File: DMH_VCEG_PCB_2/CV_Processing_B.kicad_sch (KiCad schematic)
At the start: 58 parts, among them J26 Conn_01x10_PinHeader, Q27 BC558, Q28 BC558, Q29 BC548, Q30 BC548, Q31 BC548, Q32 BC548, U18 TL074, U19 TL074, U20 TL074

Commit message: Synced PCB 2 project with PCB 1
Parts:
- J26: footprint Connector_PinHeader_2.54mm:PinHeader_1x10_P2.54mm_Vertical -> Connector_PinSocket_2.54mm:PinSocket_1x10_P2.54mm_Vertical

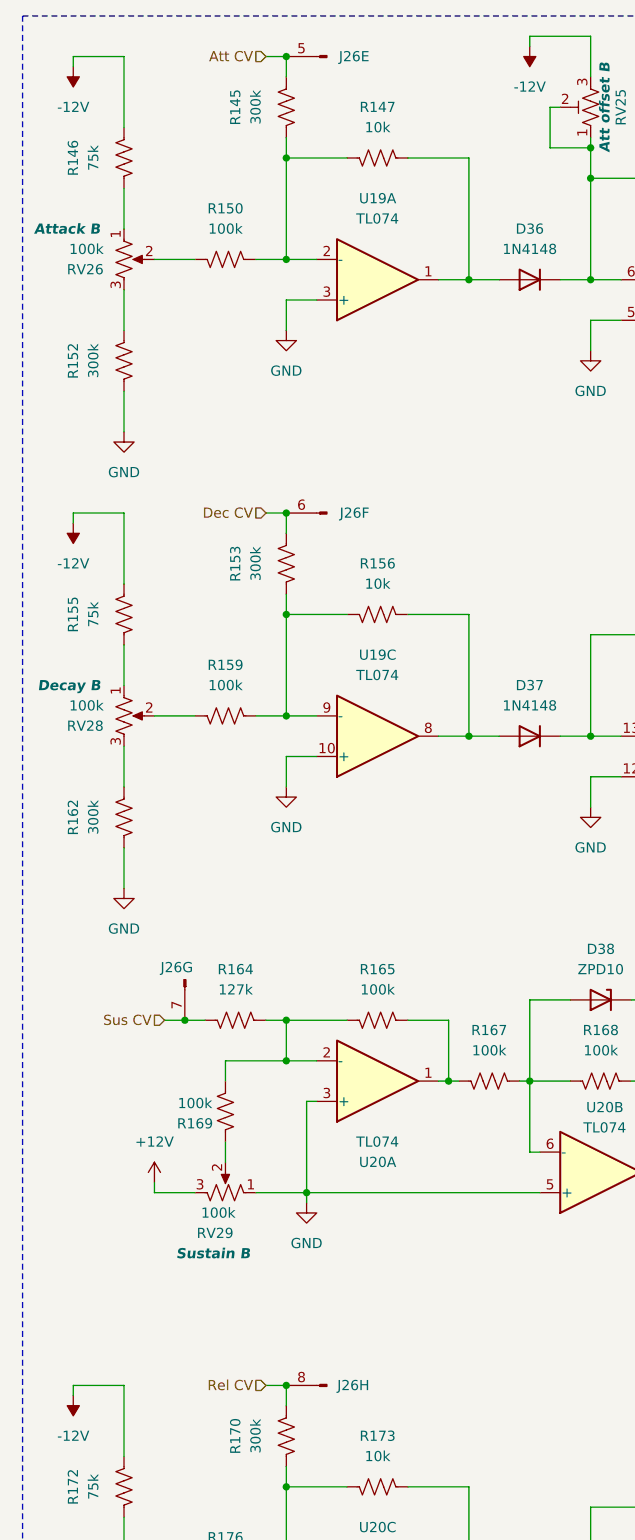
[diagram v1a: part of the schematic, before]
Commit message: PCB 2 placement in progress
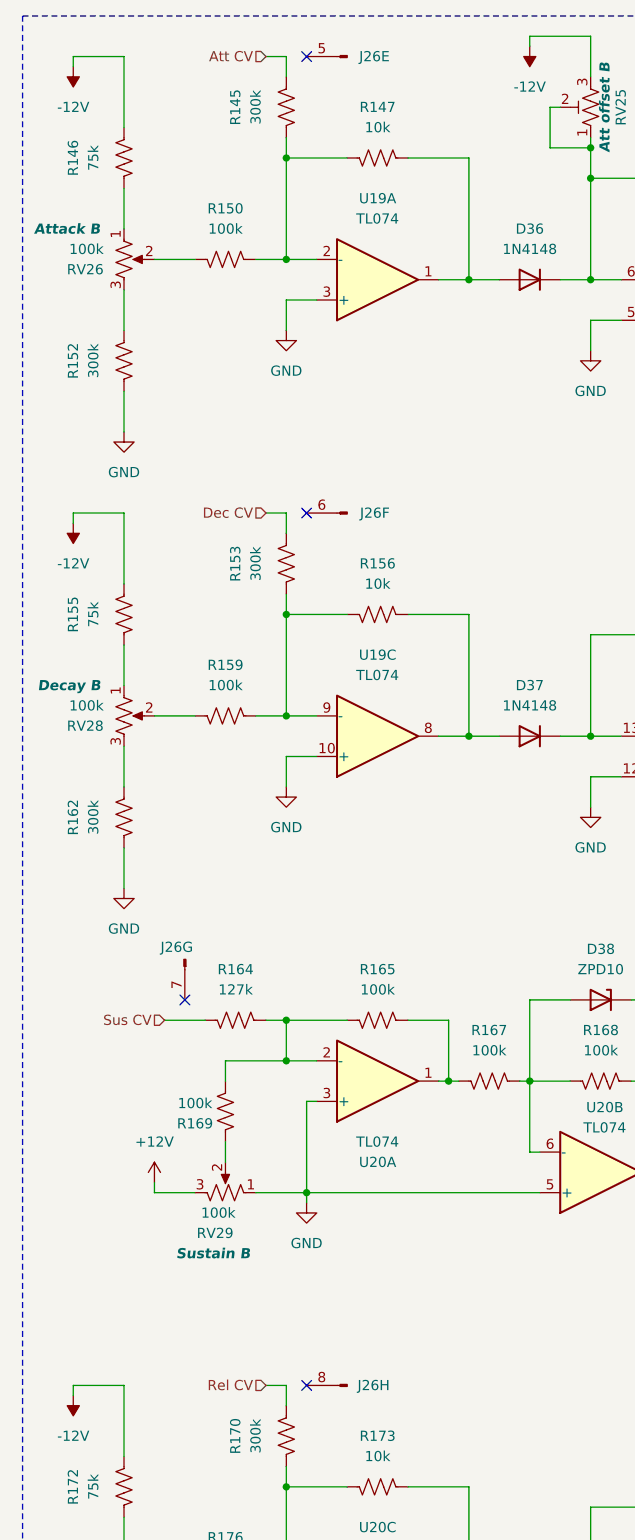
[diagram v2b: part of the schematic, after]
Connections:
- net Att CV: no longer J26.5 (Pin_5)
- net Dec CV: no longer J26.6 (Pin_6)
- net Rel CV: no longer J26.8 (Pin_8)
- net Sus CV: no longer J26.7 (Pin_7)
- no-connect marks 0 -> 4

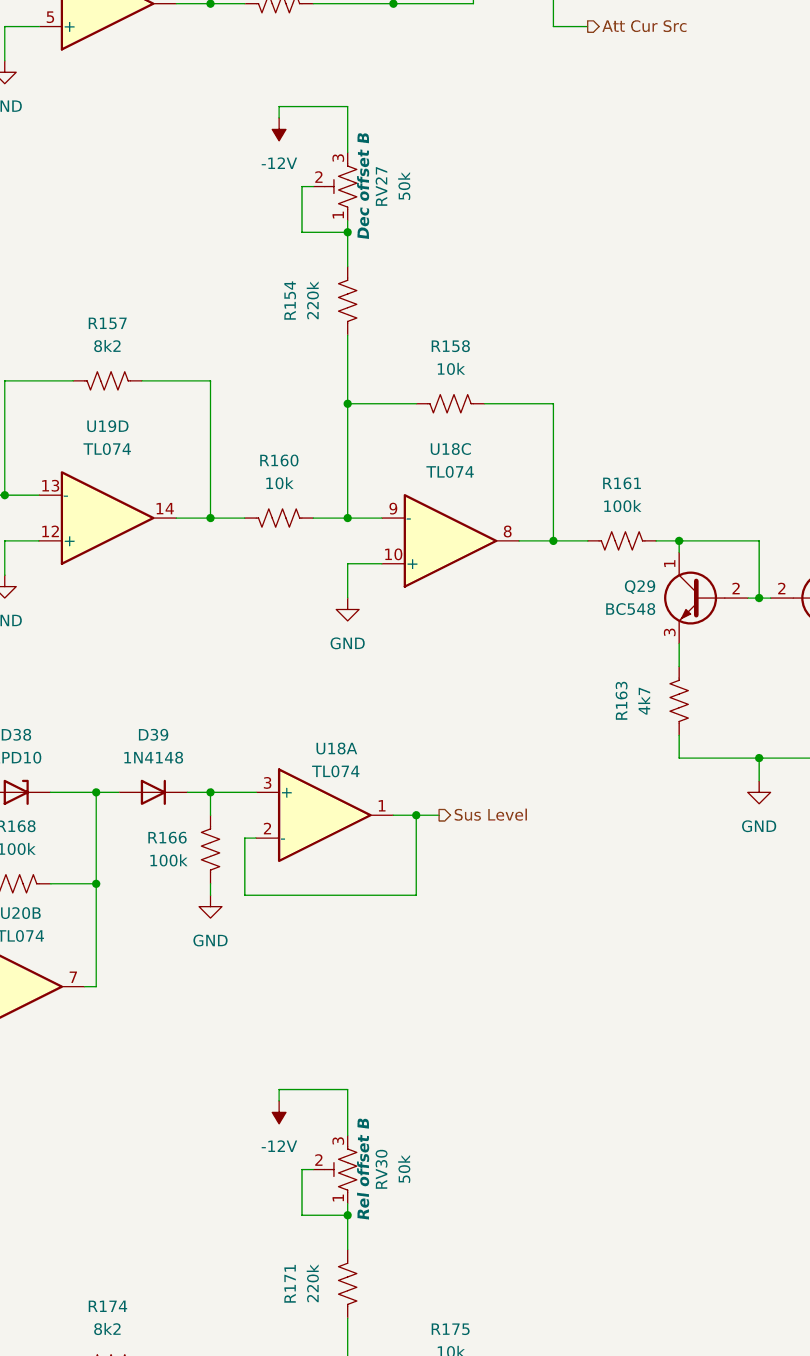
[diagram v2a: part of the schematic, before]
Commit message: Updated Dec and Rel trimpots to 100k
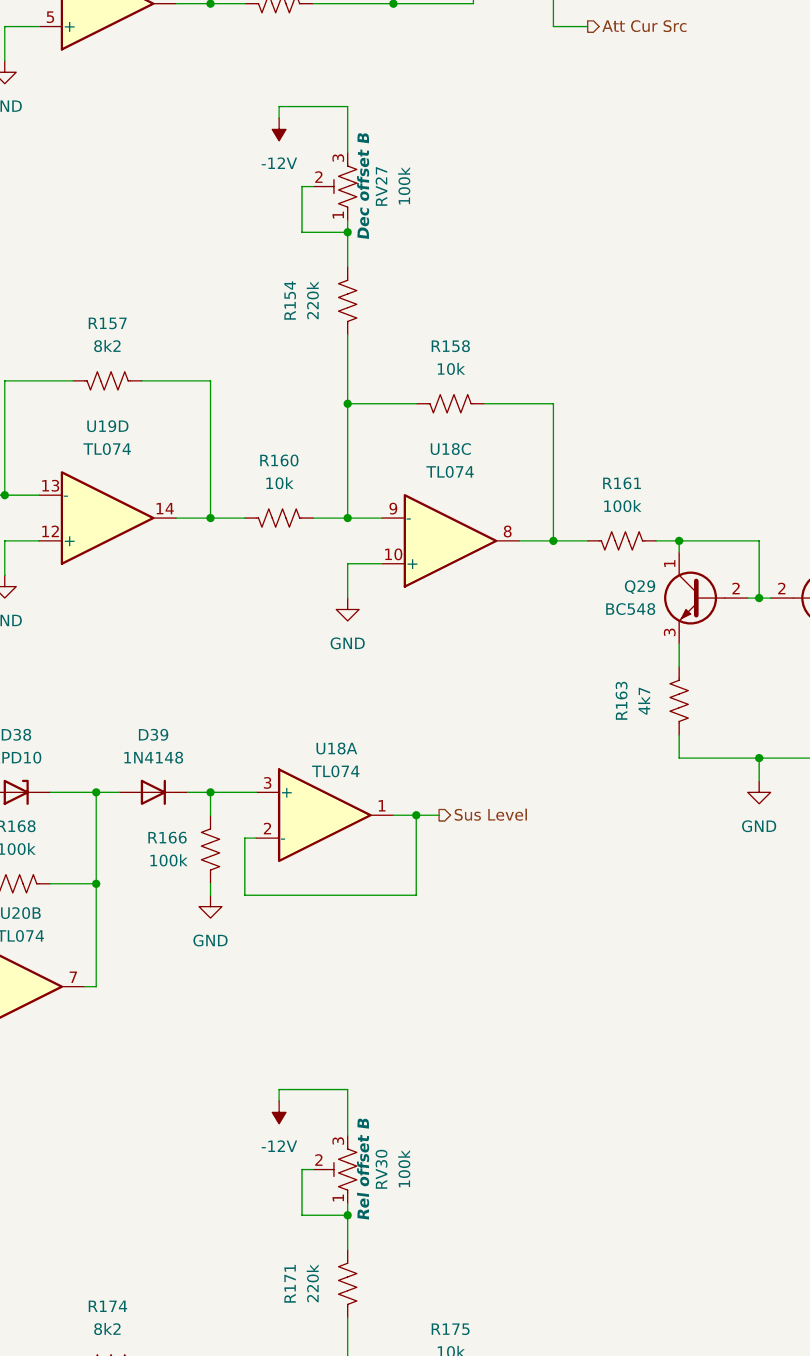
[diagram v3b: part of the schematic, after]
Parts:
- RV27, RV30: value 50k -> 100k
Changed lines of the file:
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@@
 			)
 		)
-		(property "Value" "50k"
+		(property "Value" "100k"
 			(at 128.27 69.85 90)
 			(effects
@@
 			)
 		)
-		(property "Value" "50k"
+		(property "Value" "100k"
 			(at 128.27 179.07 90)
 			(effects

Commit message: PCB 2 placement ongoing
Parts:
- D38: value ZPD10 -> Z10
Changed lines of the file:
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@@
 			)
 		)
-		(property "Value" "ZPD10"
+		(property "Value" "Z10"
 			(at 85.09 133.35 0)
 			(effects

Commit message: PCB 2 routing in progress
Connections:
- net Att CV: now also J26.5 (Pin_5)
- net Dec CV: now also J26.6 (Pin_6)
- net Rel CV: now also J26.8 (Pin_8)
- net Sus CV: now also J26.7 (Pin_7)
- no-connect marks 4 -> 0
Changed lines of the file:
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@@
+	)
+	(junction
+		(at 33.02 139.7)
+		(diameter 0)
+		(color 0 0 0 0)
 	)
 	(junction
@@
 	)
 	(junction
+		(at 45.72 185.42)
+		(diameter 0)
+		(color 0 0 0 0)
+	)
+	(junction
 		(at 45.72 88.9)
 		(diameter 0)
@@
 	)
 	(junction
+		(at 45.72 76.2)
+		(diameter 0)
+		(color 0 0 0 0)
+	)
+	(junction
 		(at 167.64 224.79)
 		(diameter 0)
@@
 	)
 	(junction
+		(at 45.72 19.05)
+		(diameter 0)
+		(color 0 0 0 0)
+	)
+	(junction
 		(at 106.68 49.53)
 		(diameter 0)
@@
 		(color 0 0 0 0)
 	)
-	(no_connect
-		(at 48.26 185.42)
-	)
-	(no_connect
-		(at 48.26 19.05)
-	)
-	(no_connect
-		(at 33.02 137.16)
-	)
-	(no_connect
-		(at 48.26 76.2)
-	)
 	(wire
 		(pts
@@
 	(wire
 		(pts
-			(xy 30.48 139.7) (xy 35.56 139.7)
+			(xy 30.48 139.7) (xy 33.02 139.7)
 		)
 		(stroke
@@
 	(wire
 		(pts
+			(xy 45.72 76.2) (xy 48.26 76.2)
+		)
+		(stroke
+			(width 0)
+			(type default)
+		)
+	)
+	(wire
+		(pts
 			(xy 129.54 139.7) (xy 127 139.7)
 		)
@@
 	(wire
 		(pts
+			(xy 45.72 185.42) (xy 48.26 185.42)
+		)
+		(stroke
+			(width 0)
+			(type default)
+		)
+	)
+	(wire
+		(pts
 			(xy 158.75 242.57) (xy 167.64 242.57)
 		)
@@
 	(wire
 		(pts
+			(xy 45.72 19.05) (xy 48.26 19.05)
+		)
+		(stroke
+			(width 0)
+			(type default)
+		)
+	)
+	(wire
+		(pts
 			(xy 116.84 69.85) (xy 116.84 74.93)
 		)
@@
 	(wire
 		(pts
+			(xy 33.02 139.7) (xy 35.56 139.7)
+		)
+		(stroke
+			(width 0)
+			(type default)
+		)
+	)
+	(wire
+		(pts
 			(xy 87.63 109.22) (xy 83.82 109.22)
 		)
@@
 		)
 		(stroke
+			(width 0)
+			(type default)
+		)
+	)
+	(wire
+		(pts
+			(xy 33.02 137.16) (xy 33.02 139.7)
+		)
+		(stroke

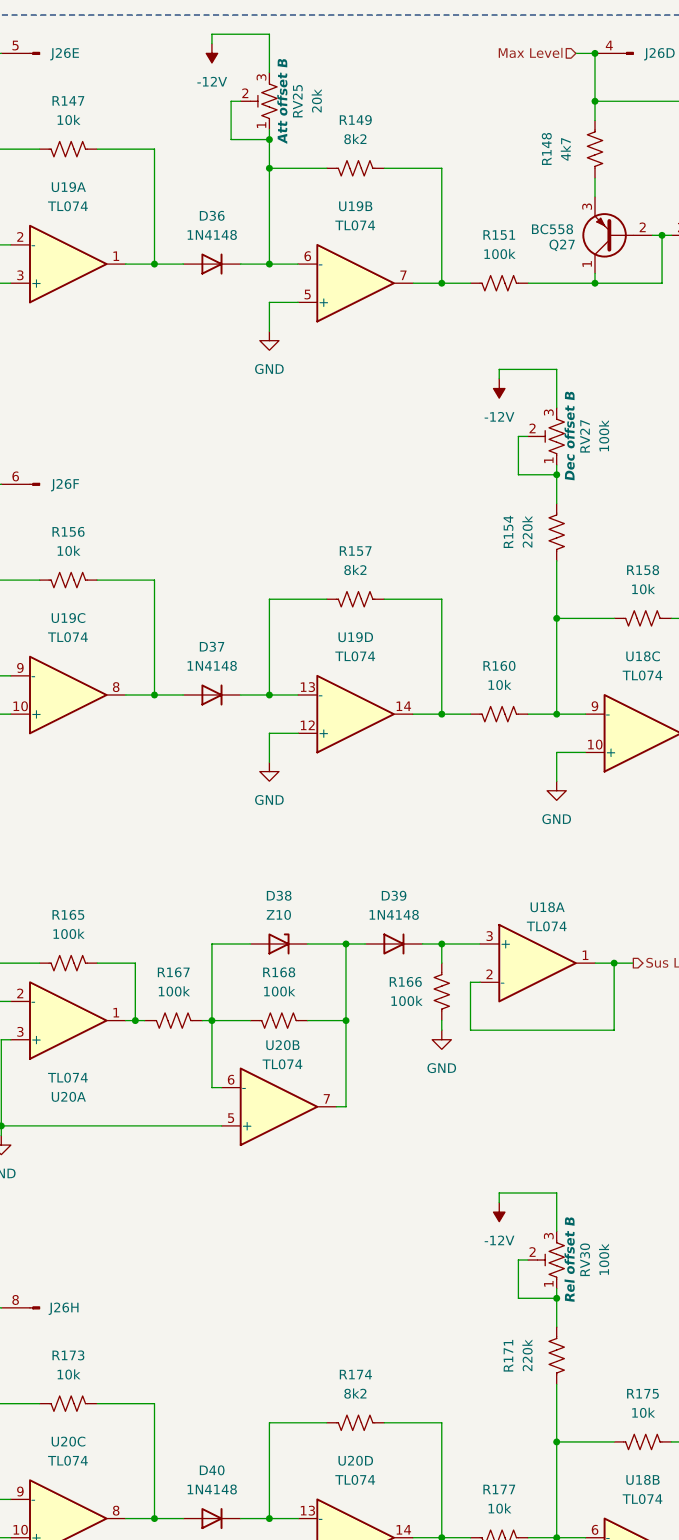
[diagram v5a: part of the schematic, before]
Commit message: Synced PCB 1 and 2
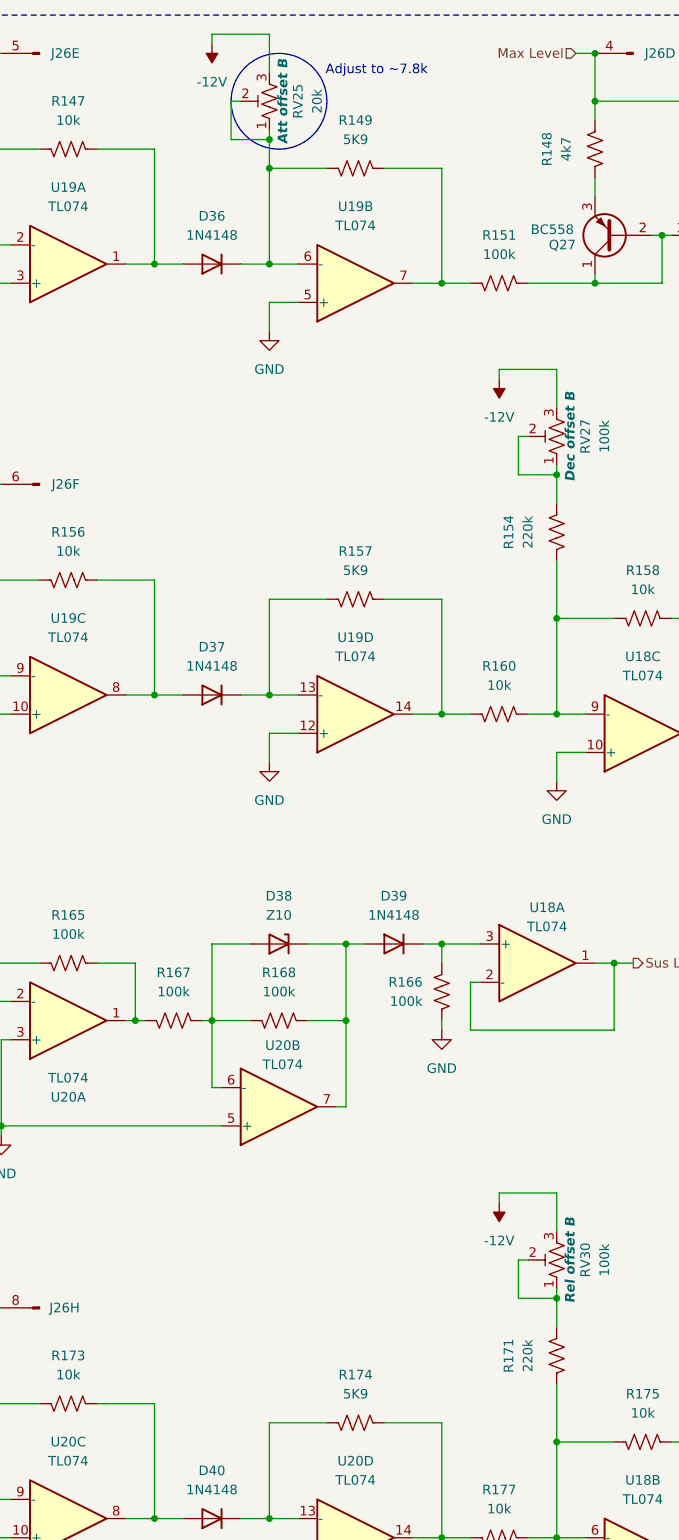
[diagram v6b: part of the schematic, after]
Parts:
- R149, R157, R174: value 8k2 -> 5K9
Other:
- note added: "Adjust to ~7.8k"
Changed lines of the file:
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@@
 		)
 	)
+	(circle
+		(center 85.09 25.4)
+		(radius 6.35)
+		(stroke
+			(width 0)
+			(type default)
+		)
+		(fill
+			(type none)
+		)
+	)
 	(text "PCB 2"
 		(exclude_from_sim no)
@@
 		)
 	)
+	(text "Adjust to ~7.8k"
+		(exclude_from_sim no)
+		(at 98.044 21.336 0)
+		(effects
+			(font
+				(size 1.27 1.27)
+			)
+		)
+	)
 	(junction
 		(at 167.64 242.57)
@@
 			)
 		)
-		(property "Value" "8k2"
+		(property "Value" "5K9"
 			(at 95.25 87.63 90)
 			(effects
@@
 			)
 		)
-		(property "Value" "8k2"
+		(property "Value" "5K9"
 			(at 95.25 196.85 90)
 			(effects
@@
 			)
 		)
-		(property "Value" "8k2"
+		(property "Value" "5K9"
 			(at 95.25 30.48 90)
 			(effects
